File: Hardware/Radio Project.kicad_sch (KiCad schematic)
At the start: 26 parts, among them SW1 208-4, U3 STM32F407VGT6

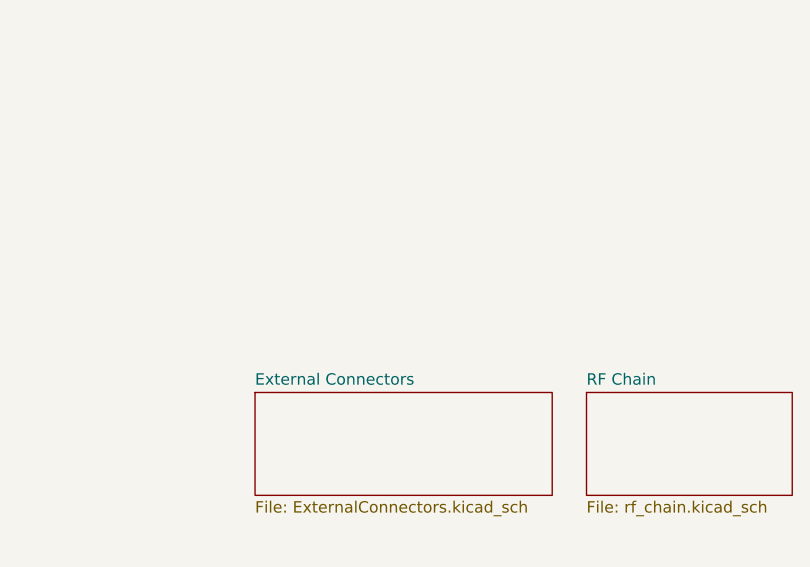
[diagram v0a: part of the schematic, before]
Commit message: Ethernet PHY and RJ45 connector
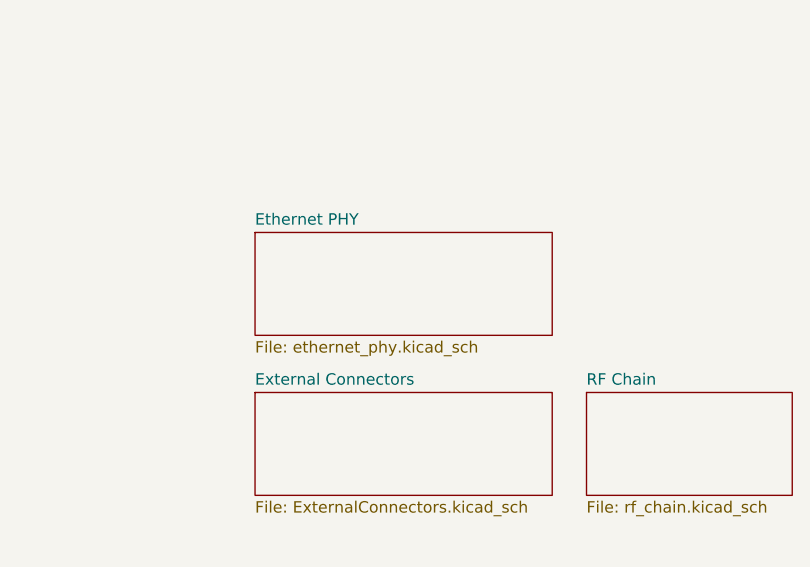
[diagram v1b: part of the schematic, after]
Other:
- added sheet Ethernet PHY (ethernet_phy.kicad_sch)
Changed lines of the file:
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@@
+	)
+	(sheet
+		(at 195.58 132.08)
+		(size 33.02 11.43)
+		(exclude_from_sim no)
+		(in_bom yes)
+		(on_board yes)
+		(dnp no)
+		(fields_autoplaced yes)
+		(stroke
+			(width 0.1524)
+			(type solid)
+		)
+		(fill
+			(color 0 0 0 0.0000)
+		)
+		(property "Sheetname" "Ethernet PHY"
+			(at 195.58 131.3684 0)
+			(effects
+				(font
+					(size 1.27 1.27)
+				)
+				(justify left bottom)
+			)
+		)
+		(property "Sheetfile" "ethernet_phy.kicad_sch"
+			(at 195.58 144.0946 0)
+			(effects
+				(font
+					(size 1.27 1.27)
+				)
+				(justify left top)
+			)
+		)
+		(instances
+			(project "Radio Project"
+				(path "/ca6389fe-9846-40e3-87a4-456cfcfc0777"
+					(page "5")
+				)
+			)
+		)
 	)
 	(sheet

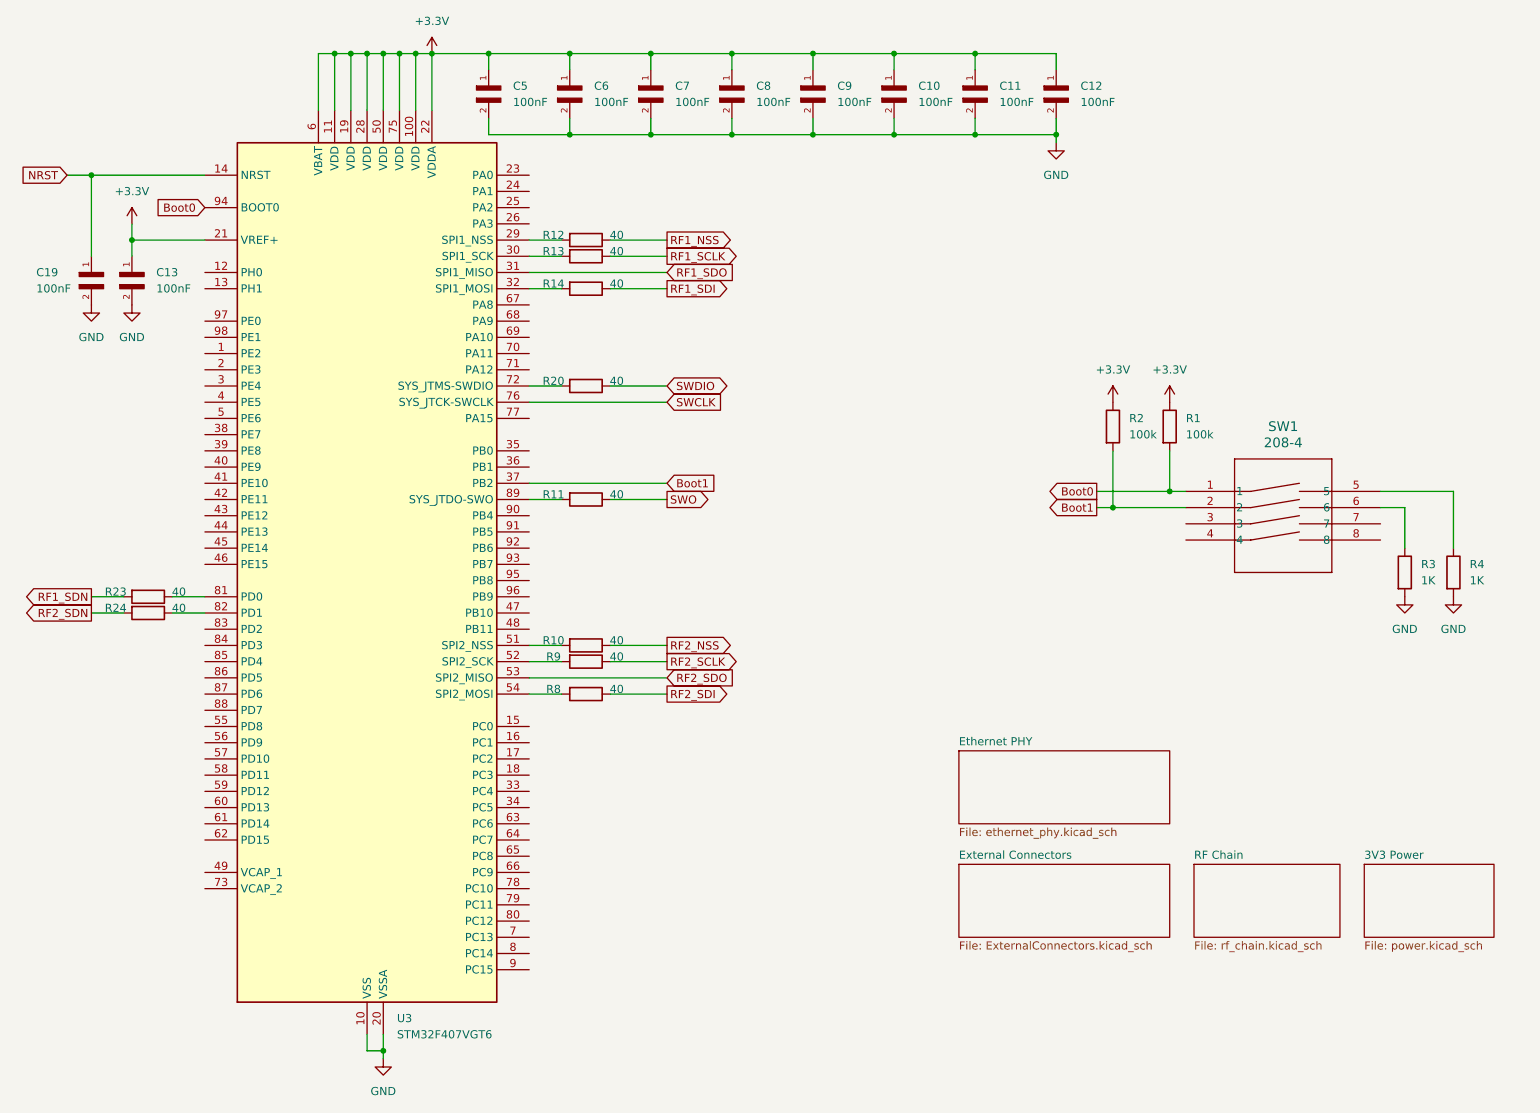
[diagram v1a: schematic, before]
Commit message: Finished Ethernet connection between MAC and PHY
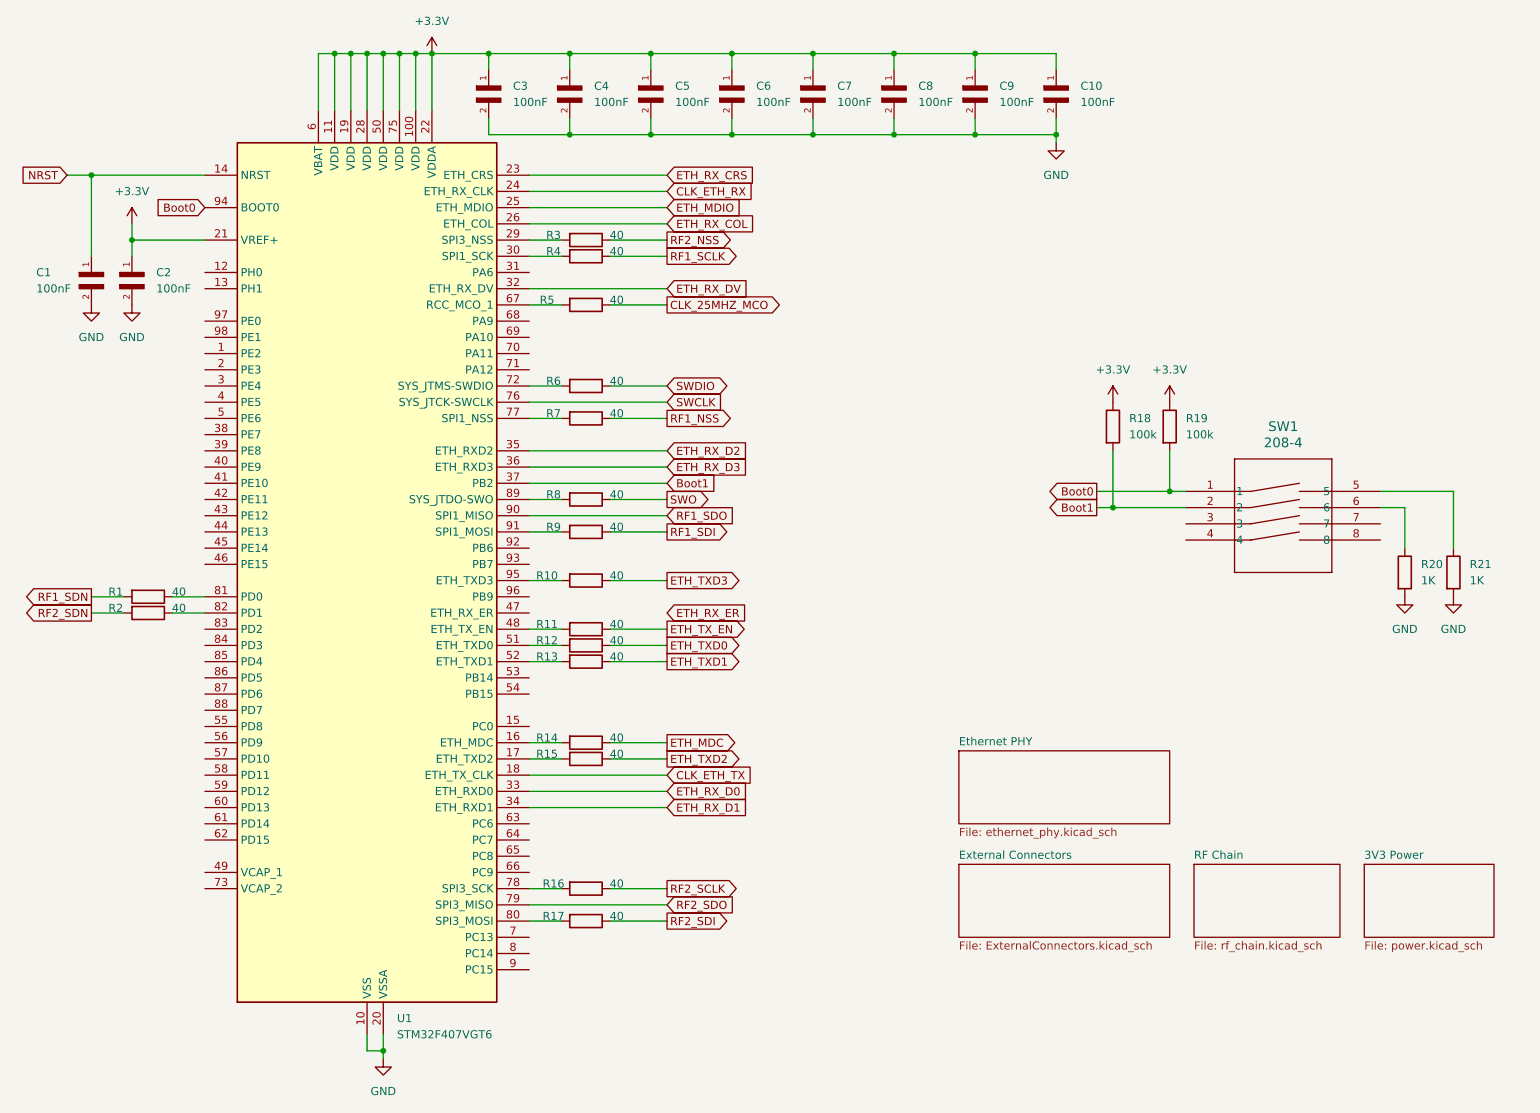
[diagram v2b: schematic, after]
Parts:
- added R10, R11, R12, R13, R14, R15, R5: 40, Resistor_SMD:R_0402_1005Metric, symbol Device:R
- renumbered C19 to C1, C12 to C10, C13 to C2, C5 to C3, C6 to C4, C7 to C5, C8 to C6, C9 to C7, C10 to C8, C11 to C9, R23 to R1, R9 to R16, R8 to R17, R2 to R18, R1 to R19, R24 to R2, R3 to R20, R4 to R21, R10 to R3, R13 to R4, R20 to R6, R12 to R7, R11 to R8, R14 to R9, U3 to U1
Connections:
- net RF1_SDO: now also U1.90 (PB4); no longer U1.31 (PA6)
- net RF2_SDO: now also U1.79 (PC11); no longer U1.53 (PB14)
- net at R3.2: now also U1.29 (PA4); no longer U1.51 (PB12)
- net at R16.2: now also U1.78 (PC10); no longer U1.52 (PB13)
- net at R17.2: now also U1.80 (PC12); no longer U1.54 (PB15)
- net at R9.2: now also U1.91 (PB5); no longer U1.32 (PA7)
- net at R7.2: now also U1.77 (PA15); no longer U1.29 (PA4)
- net at U1.16 (PC1): now also R14.2
- net at U1.17 (PC2): now also R15.2
- net CLK_ETH_TX: now reaches U1.18 (PC3)
- net ETH_RX_CRS: now reaches U1.23 (PA0)
- net CLK_ETH_RX: now reaches U1.24 (PA1)
- net ETH_MDIO: now reaches U1.25 (PA2)
- net ETH_RX_COL: now reaches U1.26 (PA3)
- net ETH_RX_D0: now reaches U1.33 (PC4)
- net ETH_RX_D1: now reaches U1.34 (PC5)
- net ETH_RX_D2: now reaches U1.35 (PB0)
- net ETH_RX_D3: now reaches U1.36 (PB1)
- net at U1.48 (PB11): now also R11.2
- net at U1.67 (PA8): now also R5.2
- net at U1.95 (PB8): now also R10.2
- new net: R12.2, U1.51 (PB12)
- new net: R13.2, U1.52 (PB13)
- new net CLK_25MHZ_MCO: R5.1
- new net ETH_MDC: R14.1
- new net ETH_RX_DV: U1.32 (PA7)
- new net ETH_TXD0: R12.1
- new net ETH_TXD1: R13.1
- new net ETH_TXD2: R15.1
- new net ETH_TXD3: R10.1
- new net ETH_TX_EN: R11.1
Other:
- moved on the sheet: R16, R17, R3, R7, R9

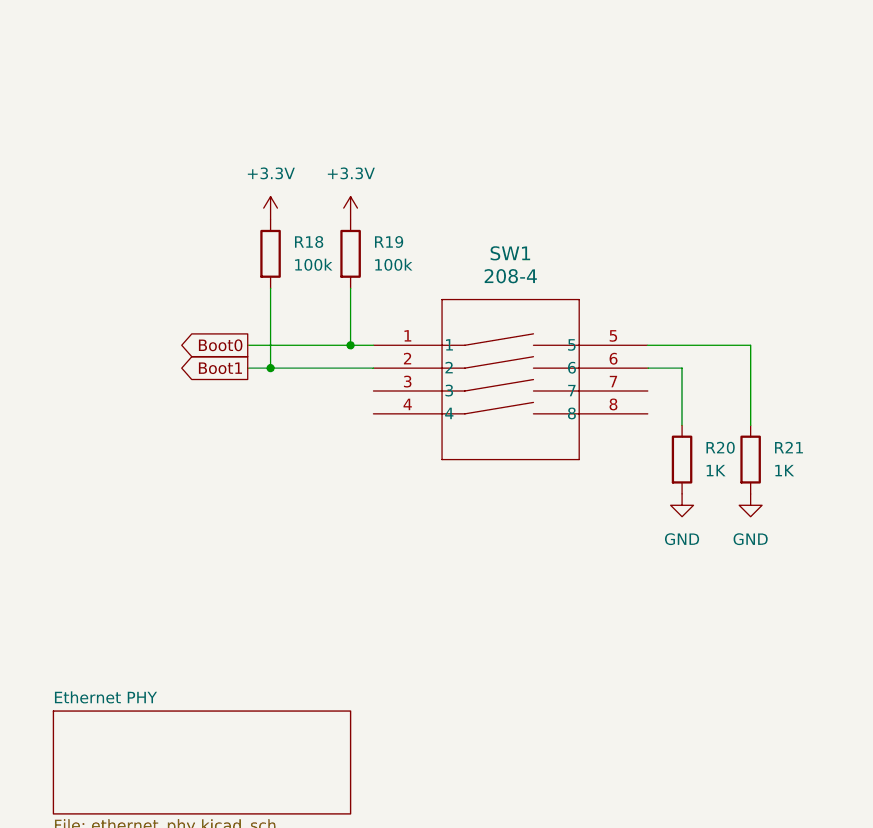
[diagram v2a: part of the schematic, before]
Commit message: Added high power USB-C Connection (5V @ 3A)
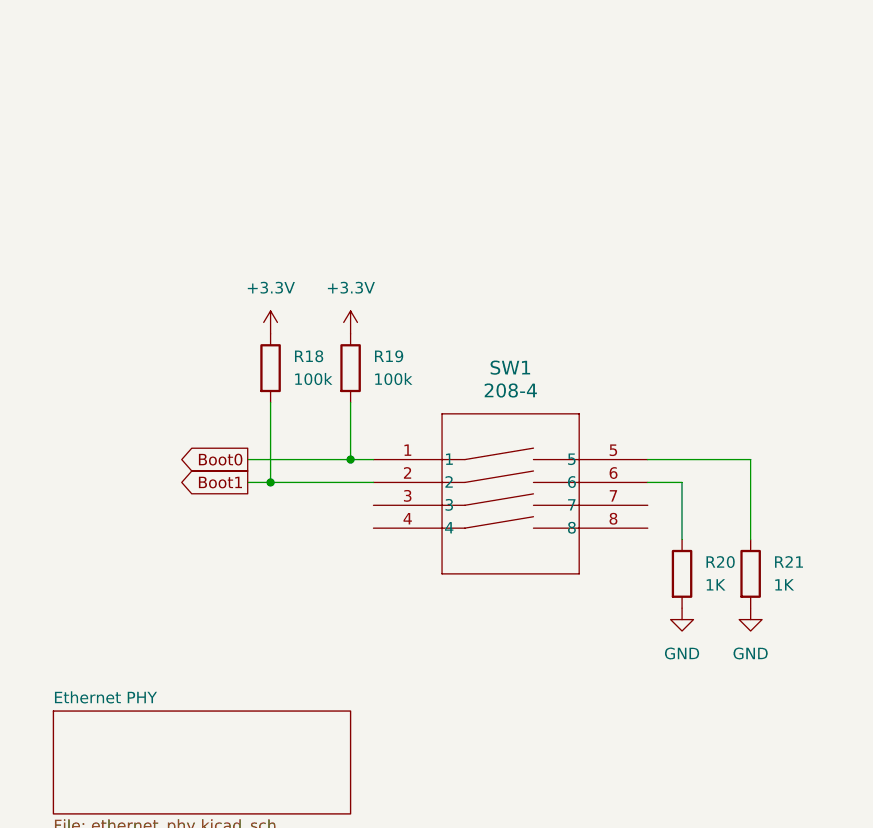
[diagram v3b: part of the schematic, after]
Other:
- moved on the sheet: R18, R19, R20, R21, SW1
